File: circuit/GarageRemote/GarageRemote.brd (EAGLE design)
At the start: 37.8 x 80 mm, 11 parts, among them U1 ESP32-DEVKITC, U2 ILQ30-X001

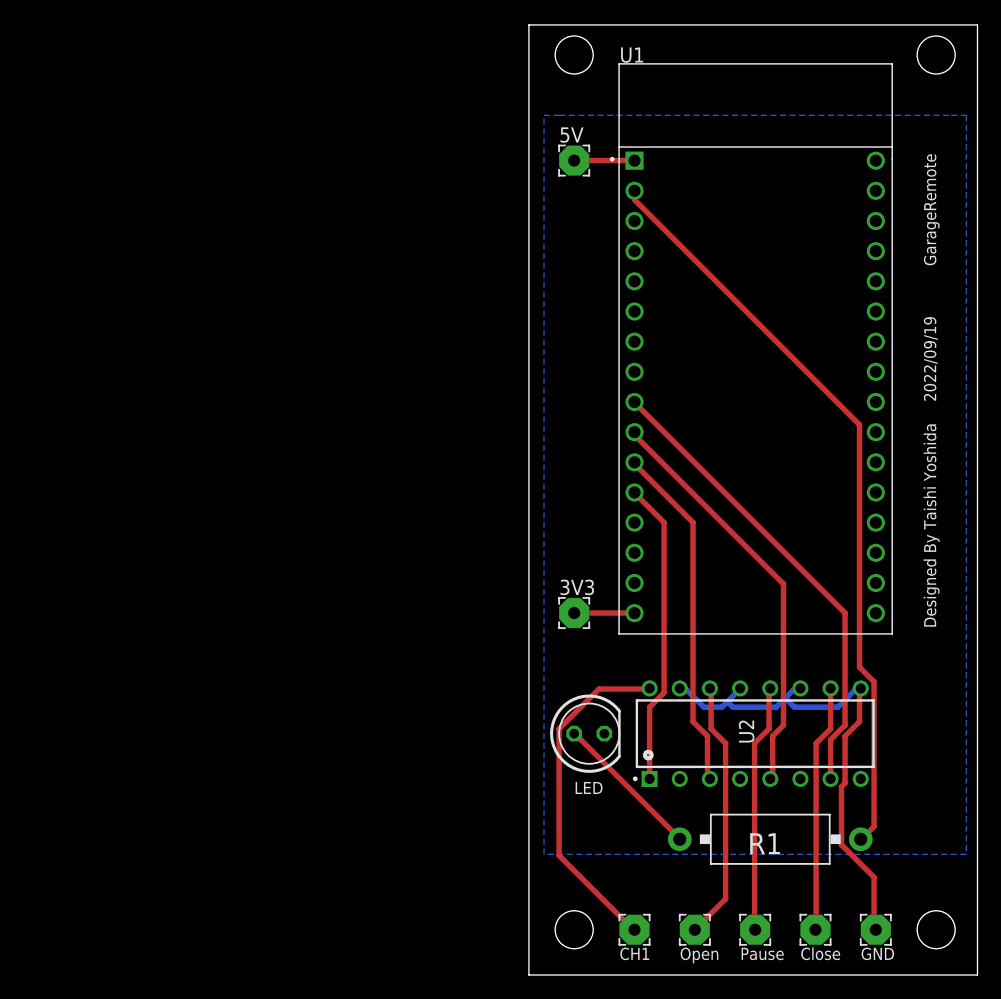
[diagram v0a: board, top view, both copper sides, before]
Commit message: Ver1.3に改修しました。
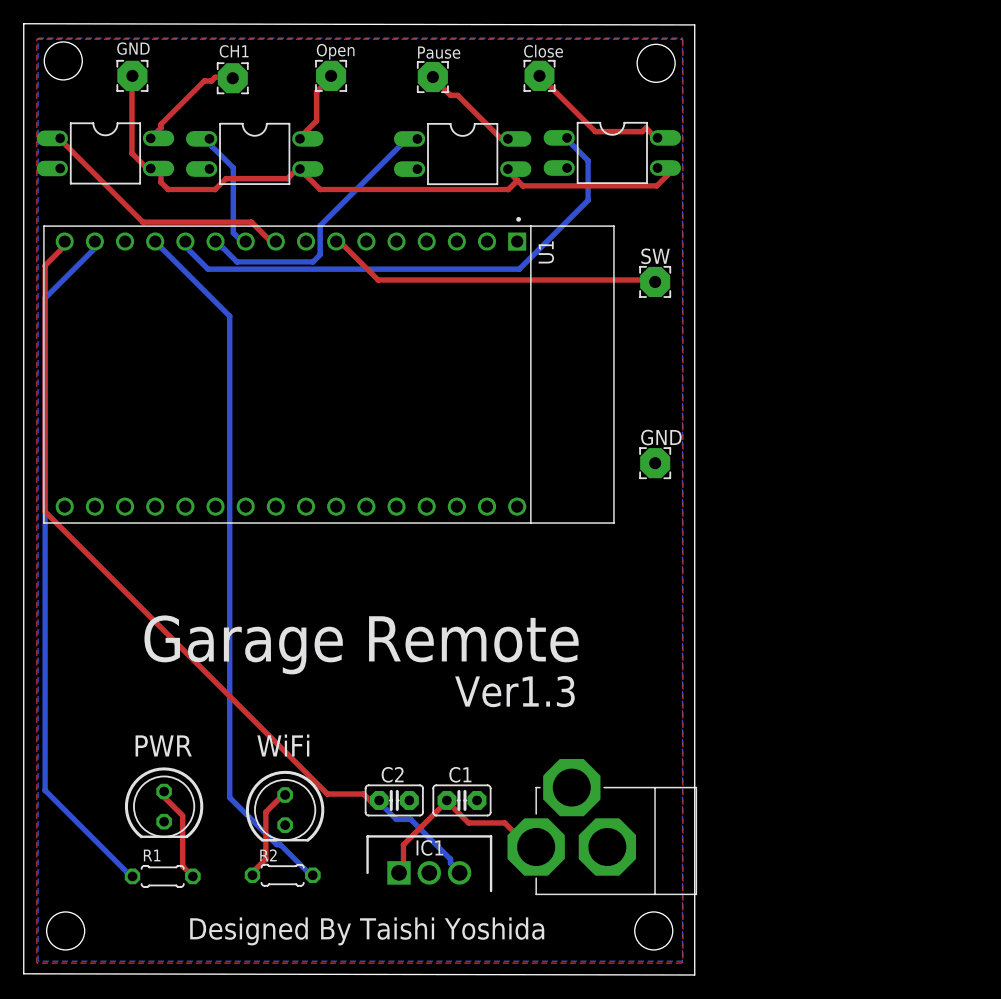
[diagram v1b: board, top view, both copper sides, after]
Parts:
- removed 3V3, 5V: (no value), wirepad:2,54/1,0
- removed U2: ILQ30-X001, ILQ30-X001:DIP762W51P254L1992H425Q16
- added C1: 0.1uF, capacitor-wima:C2.5-2
- added C2: 0.33uF, capacitor-wima:C2.5-2
- added GND, SW: (no value), wirepad:2,54/1,0
- added IC1: L7805CV, L7805CV:TO255P460X1020X2008-3P
- added LED2: (no value), led:LED5MM
- added OK1, OK2, OK3, OK4: PC817, optocoupler:DIL04
- added R2: (no value), resistor:0204/5
- added X1: (no value), power-jack:DC-21MM
- R1: device resistor-power:CA0001 -> resistor:0204/5
- U1: device ESP32-DEVKITC:MODULE_ESP32-DEVKITC -> AE-ESP32-WROOM-32E-MINI:MODULE_ESP32-DEVKITC
- moved PAD_GND 95.3 mm to (32.6, 75.7)
- moved PAD_CH1 79.3 mm to (41.1, 75.5)
- moved PAD_OPEN 78.2 mm to (49.4, 75.7)
- moved PAD_PAUSE 76.8 mm to (58.0, 75.6)
- moved PAD_CLOSE 75.6 mm to (66.9, 75.7)
- moved R1 51.3 mm to (35.2, 8.30), turned to 180 degrees
- moved U1 45.6 mm to (42.2, 49.1), turned to 270 degrees
- moved LED1 36.3 mm to (35.3, 14.2), turned to 270 degrees
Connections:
- removed net GND2: U1.23
- removed net IO13: R1.2, U1.2
- removed net N$9 (its old number): 3V3.1, U1.16
- new net 3V3: U1.1
- new net 5V: C2.1, IC1.3, U1.16
- new net BT_OFF_LED: R2.2, U1.13
- new net BT_ON_LED: R1.2, U1.15
- new net N$6: SW.1, U1.7
- new net N$7: LED2.A, R2.1
- net CH1: now also OK1.1, U1.9; no longer U1.12, U2.1
- net CLOSE: now also OK4.1, U1.12; no longer U1.9, U2.7
- net GND: now also C1.2, C2.2, GND.1, IC1.2, LED2.K, OK1.2, OK2.2, OK3.2, OK4.2, U1.14, U1.17, U1.23, X1.1, X1.3; no longer U1.29, U1.3, U2.2, U2.4, U2.6, U2.8
- net N$1: now also OK1.3, OK2.3, OK3.3, OK4.3; no longer U2.11, U2.13, U2.15, U2.9
- net N$2: now also OK2.4; no longer U2.14
- net N$3: now also OK1.4; no longer U2.16
- net N$4: now also OK3.4; no longer U2.12
- net N$5: now also OK4.4; no longer U2.10
- net N$8: now also C1.1, IC1.1, X1.2; no longer 5V.1, U1.1
- net OPEN: now also OK2.1, U1.10; no longer U1.11, U2.3
- net PAUSE: now also OK3.1, U1.11; no longer U1.10, U2.5
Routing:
- net 5V: track 0.00 -> 71.4 mm
- net IO13: track 63.4 -> 0.00 mm
- net BT_OFF_LED: track 0.00 -> 59.4 mm
- net BT_ON_LED: track 0.00 -> 58.5 mm
- net N$6: track 0.00 -> 28.3 mm
- net N$3: track 28.6 -> 9.23 mm
- net OPEN: track 29.3 -> 10.4 mm
- net N$2: track 22.0 -> 6.36 mm
- net N$1: track 43.4 -> 58.4 mm
- net N$4: track 20.9 -> 8.55 mm
- net N$8: track 5.08 -> 17.0 mm
- net PAUSE: track 34.8 -> 23.8 mm
- net N$5: track 20.8 -> 12.4 mm
- net N$7: track 0.00 -> 8.27 mm
- net N$9 (its old number): track 5.08 -> 0.00 mm
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- added copper zone on layer 1, net GND
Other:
- board size 37.8 x 80 mm -> 56.5 x 80.1 mm
- board text added: "Garage Remote"
- board text added: "PWR"
- board text added: "Ver1.3"
- board text added: "WiFi"
- board text removed: "2022/09/19"
- board text removed: "GarageRemote"
- board text removed: "LED"
